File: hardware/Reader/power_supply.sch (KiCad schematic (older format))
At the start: 5 parts

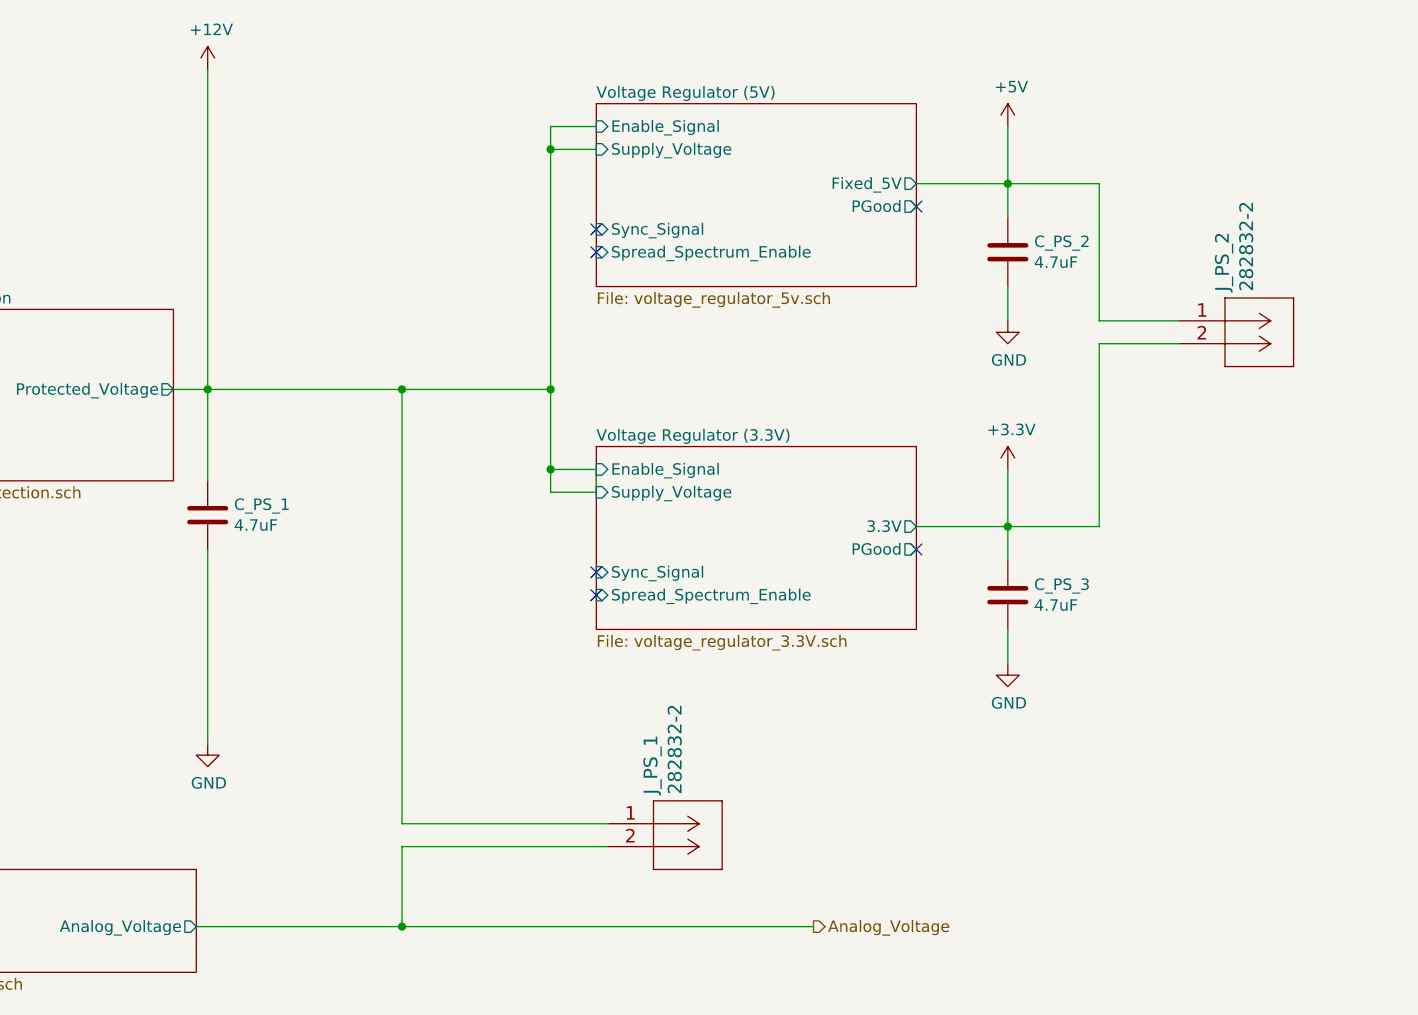
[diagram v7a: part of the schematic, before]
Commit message: Fixed bugs in schematic. Updated BOM list. Swapped to using ESP32 holder. Updated PCB layout to v0.0.2. Updated schematic to v0.0.4
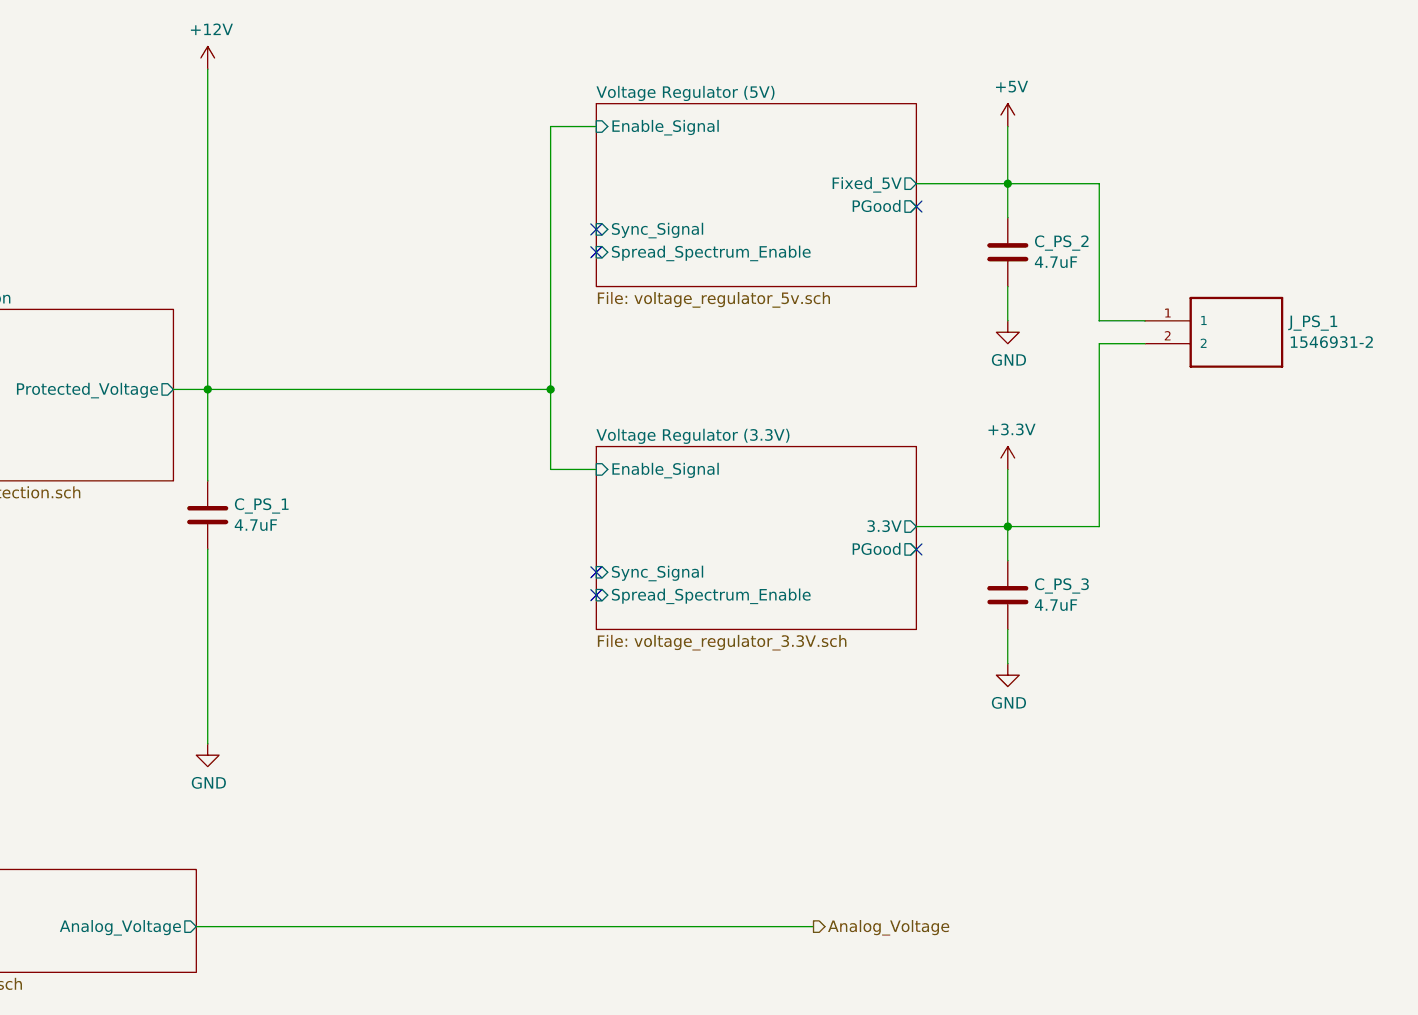
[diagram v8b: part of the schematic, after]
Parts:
- removed J_PS_1, J_PS_2: 282832-2, footprints:282832-2, symbol 2828322:282832-2
- added J_PS_1: 1546931-2, footprints:1546931-2, symbol 1546931-2:1546931-2
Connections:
- wire segments 37 -> 26
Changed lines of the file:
@@
 Sheet 15 19
 Title "CANnect Reader | Power Supply"
-Date "2020-10-27"
-Rev "0.0.03"
+Date "2020-10-28"
+Rev "0.0.04"
 Comp "CANtech"
 Comment1 "Created by Choong Jin Ng | jin8383@gmail.com"
@@
 $EndComp
 Wire Wire Line
-	3150 2800 3350 2800
-Wire Wire Line
 	3350 3200 3350 2800
 Connection ~ 3350 2800
@@
 	1100 2800 1700 2800
 Wire Wire Line
-	4850 2800 4850 1750
-Wire Wire Line
 	4850 1650 5050 1650
-Wire Wire Line
-	5050 1750 4850 1750
-Connection ~ 4850 1750
-Wire Wire Line
-	4850 1750 4850 1650
 Wire Wire Line
 	4850 2800 4850 3150
@@
 	4850 3150 5050 3150
 Connection ~ 4850 2800
-Wire Wire Line
-	5050 3150 5050 3250
-Wire Wire Line
-	4850 3150 4850 3250
-Wire Wire Line
-	4850 3250 5050 3250
-Connection ~ 4850 3150
 NoConn ~ 5050 3600
 NoConn ~ 5050 3700
@@
 	1    0    0    -1
 $EndComp
-$Comp
-L 2828322:282832-2 J_PS_1
-U 1 1 5F928400
-P 5100 4700
-F 0 "J_PS_1" V 5289 4828 60  0000 L CNN
-F 1 "282832-2" V 5395 4828 60  0000 L CNN
-F 2 "footprints:282832-2" H 5500 4640 60  0001 C CNN
-F 3 "https://www.te.com/commerce/DocumentDelivery/DDEController?Action=srchrtrv&DocNm=282832&DocType=Customer+Drawing&DocLang=English" H 5100 4700 60  0001 C CNN
-F 4 "282832-2" H 5100 4700 50  0001 C CNN "Part Name"
-F 5 "DigiKey Canada" H 5100 4700 50  0001 C CNN "Vendor"
-F 6 "TE Connectivity AMP Connectors" H 5100 4700 50  0001 C CNN "Manufacturer"
-F 7 "A113314-ND" H 5100 4700 50  0001 C CNN "digikeypn"
-	1    5100 4700
-	1    0    0    -1
-$EndComp
 $Sheet
 S 1750 4900 1550 450
@@
 F2 "Analog_Voltage" O R 3300 5150 50
 $EndSheet
-Wire Wire Line
-	3300 5150 4200 5150
 Text HLabel 6000 5150 2    50   Output ~ 0
 Analog_Voltage
@@
 Connection ~ 6850 3400
 Wire Wire Line
-	7250 2600 7600 2600
-Wire Wire Line
 	7250 3400 7250 2600
 Wire Wire Line
 	6850 3400 7250 3400
 Connection ~ 6850 1900
-Wire Wire Line
-	7250 2500 7600 2500
 Wire Wire Line
 	7250 1900 7250 2500
@@
 F1 "voltage_regulator_5v.sch" 50
 F2 "Enable_Signal" I L 5050 1650 50
-F3 "Supply_Voltage" I L 5050 1750 50
-F4 "Sync_Signal" I L 5050 2100 50
-F5 "Fixed_5V" O R 6450 1900 50
-F6 "PGood" O R 6450 2000 50
-F7 "Spread_Spectrum_Enable" I L 5050 2200 50
+F3 "Sync_Signal" I L 5050 2100 50
+F4 "Fixed_5V" O R 6450 1900 50
+F5 "PGood" O R 6450 2000 50
+F6 "Spread_Spectrum_Enable" I L 5050 2200 50
 $EndSheet
 $Sheet
@@
 F1 "voltage_regulator_3.3V.sch" 50
 F2 "Enable_Signal" I L 5050 3150 50
-F3 "Supply_Voltage" I L 5050 3250 50
-F4 "Sync_Signal" I L 5050 3600 50
-F5 "3.3V" O R 6450 3400 50
-F6 "PGood" O R 6450 3500 50
-F7 "Spread_Spectrum_Enable" I L 5050 3700 50
-$EndSheet
-$Comp
-L 2828322:282832-2 J_PS_2
-U 1 1 5F9327D0
-P 7600 2500
-F 0 "J_PS_2" V 7789 2628 60  0000 L CNN
-F 1 "282832-2" V 7895 2628 60  0000 L CNN
-F 2 "footprints:282832-2" H 8000 2440 60  0001 C CNN
-F 3 "https://www.te.com/commerce/DocumentDelivery/DDEController?Action=srchrtrv&DocNm=282832&DocType=Customer+Drawing&DocLang=English" H 7600 2500 60  0001 C CNN
-F 4 "282832-2" H 7600 2500 50  0001 C CNN "Part Name"
-F 5 "DigiKey Canada" H 7600 2500 50  0001 C CNN "Vendor"
-F 6 "TE Connectivity AMP Connectors" H 7600 2500 50  0001 C CNN "Manufacturer"
-F 7 "A113314-ND" H 7600 2500 50  0001 C CNN "digikeypn"
-	1    7600 2500
-	1    0    0    -1
-$EndComp
+F3 "Sync_Signal" I L 5050 3600 50
+F4 "3.3V" O R 6450 3400 50
+F5 "PGood" O R 6450 3500 50
+F6 "Spread_Spectrum_Enable" I L 5050 3700 50
+$EndSheet
 $Comp
 L power:+5V #PWR093
@@
 $EndComp
 Wire Wire Line
-	3350 2800 4200 2800
-Wire Wire Line
-	4200 2800 4200 4700
-Wire Wire Line
-	4200 4700 5100 4700
-Connection ~ 4200 2800
-Wire Wire Line
-	4200 2800 4850 2800
-Wire Wire Line
-	5100 4800 4200 4800
-Wire Wire Line
-	4200 4800 4200 5150
-Connection ~ 4200 5150
-Wire Wire Line
-	4200 5150 6000 5150
+	4850 1650 4850 2800
+Wire Wire Line
+	3350 2800 3200 2800
+$Comp
+L 1546931-2:1546931-2 J_PS_1
+U 1 1 5FA002EC
+P 7850 2600
+F 0 "J_PS_1" H 8080 2696 50  0000 L CNN
+F 1 "1546931-2" H 8080 2605 50  0000 L CNN
+F 2 "footprints:1546931-2" H 7850 2600 50  0001 L BNN
+F 3 "https://www.te.com/commerce/DocumentDelivery/DDEController?Action=srchrtrv&DocNm=1-1773458-1_EURO_STYLE_QRG&DocType=DS&DocLang=English" H 7850 2600 50  0001 L BNN
+F 4 "1546931-2" H 7850 2600 50  0001 C CNN "Part Name"
+F 5 "TE Connectivity AMP Connectors" H 7850 2600 50  0001 C CNN "Manufacturer"
+F 6 "Digikey Canada" H 7850 2600 50  0001 C CNN "Vendor"
+F 7 "A97965-ND" H 7850 2600 50  0001 C CNN "digikeypn"
+	1    7850 2600
+	1    0    0    -1
+$EndComp
+Wire Wire Line
+	7250 2500 7450 2500
+Wire Wire Line
+	7450 2600 7250 2600
+Wire Wire Line
+	3350 2800 4850 2800
+Wire Wire Line
+	3300 5150 6000 5150
 $EndSCHEMATC
